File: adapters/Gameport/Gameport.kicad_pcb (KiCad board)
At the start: 2 copper layers, 58.4 x 35.6 mm, 20 parts, among them J1 Port 1, J2 Port 2, J3 Gameport, M1 Mounting, M2 Mounting, M3 Mounting, M4 Mounting, Q1 BC557, Q2 BC557

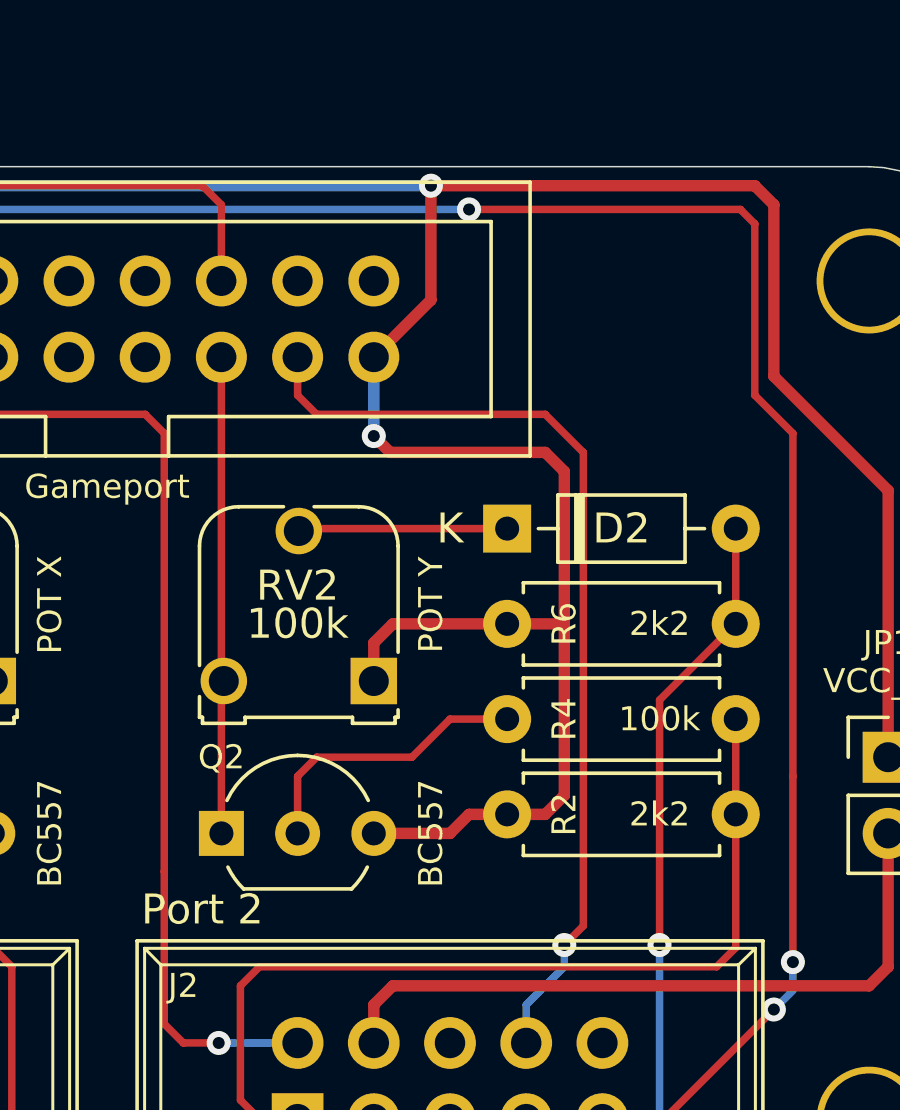
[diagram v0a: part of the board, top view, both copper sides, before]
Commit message: Fixed pin linked to VCC
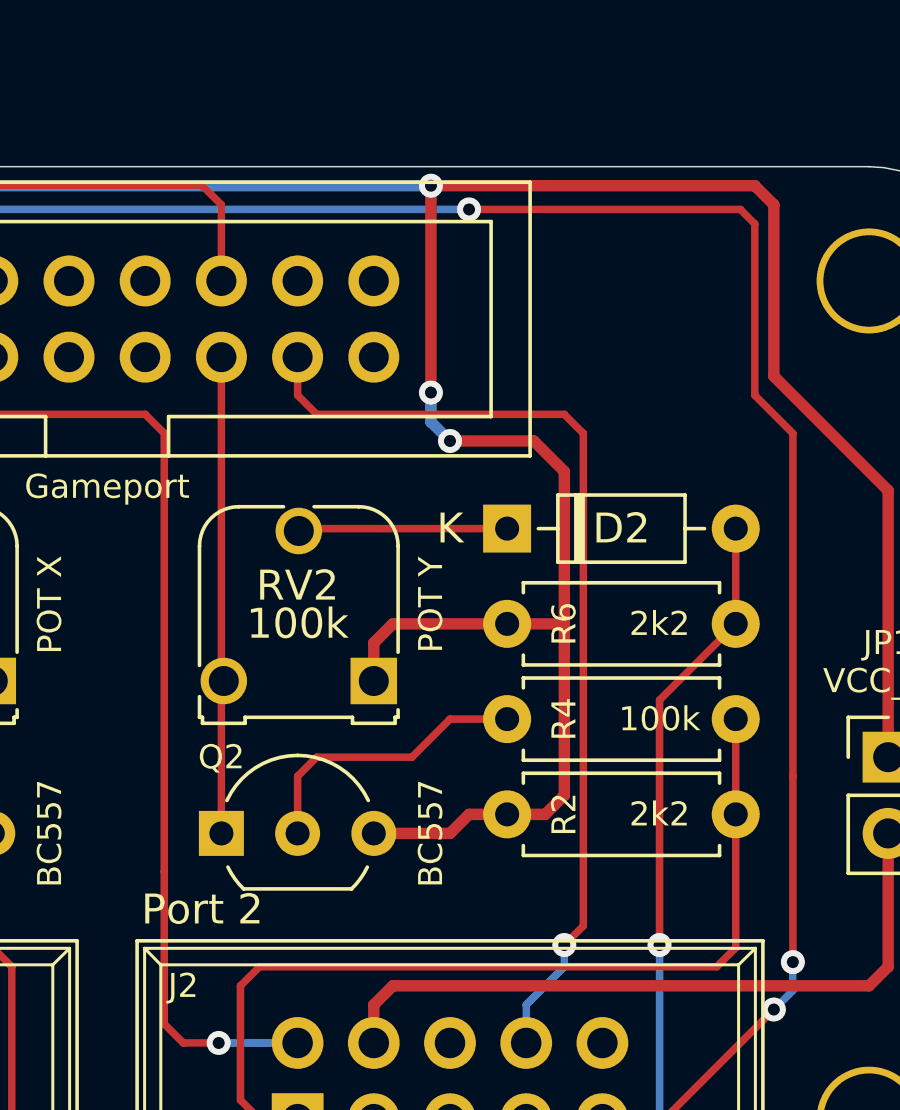
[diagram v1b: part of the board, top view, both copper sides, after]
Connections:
- J3 pad 8: VCC -> (no net)
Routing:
- net VCC: track 149.1 -> 146.1 mm, vias 2 -> 3

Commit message: Trying out different circuit
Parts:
- removed RV1, RV2: 100k, RM-065:RM-065
- added R7: 100k, resistor:R_Axial_DIN0207_L6.3mm_D2.5mm_P7.62mm_Horizontal, F.Cu at (120.0, 92.7)
- added R8: 100k, resistor:R_Axial_DIN0207_L6.3mm_D2.5mm_P7.62mm_Horizontal, F.Cu at (160.7, 92.7)
- Q1, Q2: value BC557 -> 2N3906
- R1, R2: value 2k2 -> 100k
- R5, R6: value 2k2 -> 47k
- moved R2 11.9 mm to (160.7, 86.4)
- moved R6 11.7 mm to (168.3, 95.9), turned to 180 degrees
- moved D1 7.62 mm to (130.8, 95.9), turned to 90 degrees
- moved D2 7.62 mm to (157.5, 95.9), turned to 90 degrees
- moved Q1 7.62 mm to (135.3, 90.8)
- moved Q2 7.62 mm to (148.0, 90.8)
- moved R4 5.99 mm to (160.7, 89.5)
- moved R1 5.99 mm to (120.0, 86.4)
- moved R3 5.99 mm to (120.0, 89.5)
- moved JP1 3.81 mm to (170.2, 99.7)
- moved R5 3.70 mm to (120.0, 95.9)
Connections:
- J3 pad 3: Net-(J3-Pad3) -> Net-(D1-Pad1)
- J3 pad 6: Net-(J3-Pad6) -> Net-(D2-Pad1)
- J3 pad 9: VCC -> (no net)
- Q1 pad 1: Net-(J3-Pad3) -> VCC
- Q1 pad 3: VCC -> Net-(D1-Pad1)
- Q2 pad 1: Net-(J3-Pad6) -> VCC
- Q2 pad 3: VCC -> Net-(D2-Pad1)
- R1 pad 2: /JK_LEFT -> /JK_RIGHT
- R2 pad 2: /JK_UP -> /JK_DOWN
- R3 pad 1: Net-(Q1-Pad2) -> VCC
- R3 pad 2: /JK_LEFT -> Net-(D1-Pad1)
- R4 pad 1: Net-(Q2-Pad2) -> VCC
- R4 pad 2: /JK_UP -> Net-(D2-Pad1)
- R5 pad 1: VCC -> /JK_LEFT
- R5 pad 2: /JK_RIGHT -> Net-(Q1-Pad2)
- R6 pad 1: VCC -> Net-(Q2-Pad2)
- R6 pad 2: /JK_DOWN -> /JK_UP
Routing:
- net VCC: track 146.1 -> 92.4 mm, vias 3 -> 0
- net Net-(D1-Pad1): track 7.06 -> 38.1 mm
- net Net-(D2-Pad1): track 6.98 -> 33.4 mm
- net Net-(Q2-Pad2): track 9.68 -> 29.9 mm
- net Net-(J3-Pad3): track 20.2 -> 0.00 mm
- net Net-(J3-Pad6): track 15.9 -> 0.00 mm
- net /JK_DOWN: track 33.3 -> 48.8 mm
- net /JK_FIRE3: track 64.1 -> 74.2 mm, vias 3 -> 1
- net /JK_UP: track 30.6 -> 20.7 mm
- net /JK_LEFT: track 43.2 -> 52.1 mm
- net Net-(Q1-Pad2): track 22.8 -> 14.9 mm
- net /JK_FIRE2: track 32.4 -> 37.7 mm
- net Net-(J2-Pad7): track 23.4 -> 18.9 mm
- net /JK_RIGHT: track 64.4 -> 63.6 mm, vias 0 -> 1
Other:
- board text added: "PC Gameport (C64 JoyKEY Adapter) github.com/tebl"
- board text removed: "Gameport (C64 JoyKEY Adapter) github.com/tebl"
- board text removed: "POT X"
- board text removed: "POT Y"

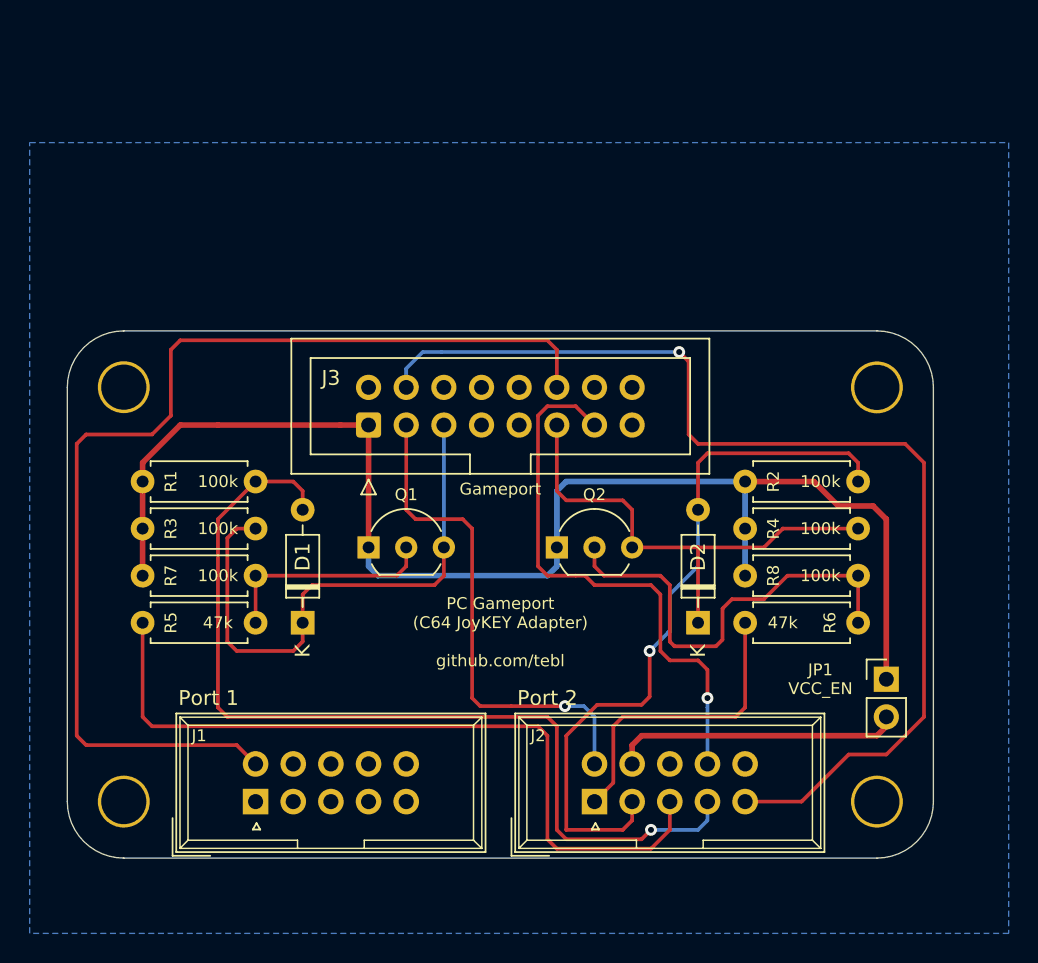
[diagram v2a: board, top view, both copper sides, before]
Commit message: Different gameport circuit
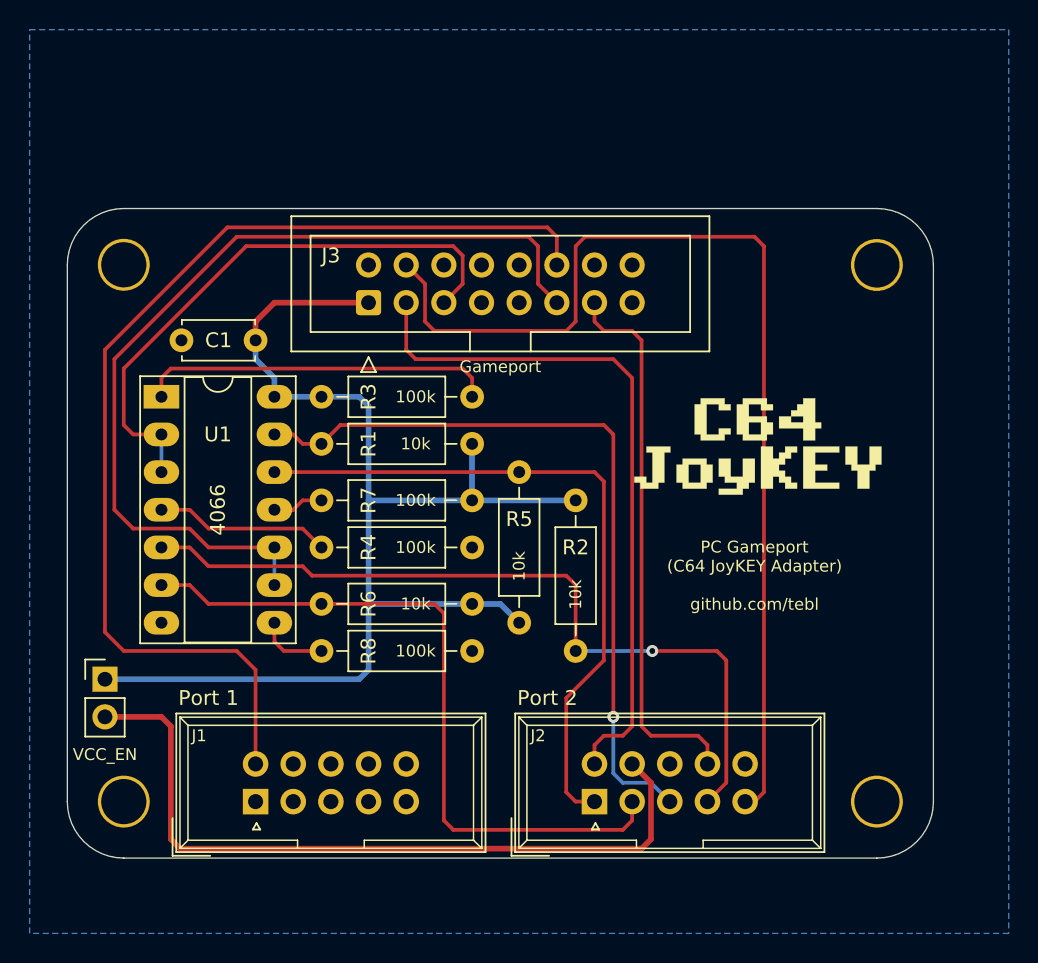
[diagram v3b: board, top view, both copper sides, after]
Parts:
- removed D1, D2: 1N4148, Diode_THT:D_DO-35_SOD27_P7.62mm_Horizontal
- removed Q1, Q2: 2N3906, Package_TO_SOT_THT:TO-92_Inline_Wide
- added C1: 100nF, Capacitor_THT:C_Disc_D4.7mm_W2.5mm_P5.00mm, F.Cu at (127.6, 76.8)
- added G***: LOGO, logo:c64_joykey, F.Cu at (161.3, 83.8)
- added U1: 4066, Package_DIP:DIP-14_W7.62mm_Socket_LongPads, F.Cu at (121.3, 80.6)
- R1, R2: value 100k -> 10k; footprint resistor:R_Axial_DIN0207_L6.3mm_D2.5mm_P7.62mm_Horizontal -> Resistor_THT:R_Axial_DIN0207_L6.3mm_D2.5mm_P10.16mm_Horizontal
- R3, R4, R7, R8: footprint resistor:R_Axial_DIN0207_L6.3mm_D2.5mm_P7.62mm_Horizontal -> Resistor_THT:R_Axial_DIN0207_L6.3mm_D2.5mm_P10.16mm_Horizontal
- R5, R6: value 47k -> 10k; footprint resistor:R_Axial_DIN0207_L6.3mm_D2.5mm_P7.62mm_Horizontal -> Resistor_THT:R_Axial_DIN0207_L6.3mm_D2.5mm_P10.16mm_Horizontal
- moved JP1 52.7 mm to (117.5, 99.7)
- moved R6 36.2 mm to (132.1, 94.6), turned to 0 degrees
- moved R5 27.4 mm to (145.4, 85.7), turned to 270 degrees
- moved R3 23.9 mm to (142.2, 80.6), turned to 180 degrees
- moved R8 19.1 mm to (142.2, 97.8), turned to 180 degrees
- moved R4 18.5 mm to (142.2, 90.8), turned to 180 degrees
- moved R2 16.2 mm to (149.2, 97.8), turned to 90 degrees
- moved R7 13.1 mm to (132.1, 87.6)
- moved R1 12.3 mm to (132.1, 83.8)
- moved M3 8.26 mm to (169.5, 71.8)
- moved J3 8.25 mm to (135.3, 74.3)
- moved M4 8.25 mm to (118.7, 71.7)
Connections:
- net /JK_FIRE1 renamed JK_FIRE1
- net /JK_FIRE2 renamed JK_FIRE2
- net /JK_FIRE3 renamed JK_FIRE3
- net /JK_FIRE4 renamed JK_FIRE4
- J2 pad 1: /JK_UP -> JK_UP
- J2 pad 2: /JK_DOWN -> JK_DOWN
- J2 pad 3: /JK_LEFT -> JK_LEFT
- J2 pad 4: /JK_RIGHT -> JK_RIGHT
- J3 pad 3: Net-(D1-Pad1) -> PC_X
- J3 pad 6: Net-(D2-Pad1) -> PC_Y
- R1 pad 1: VCC -> JK_LEFT
- R1 pad 2: /JK_RIGHT -> VCC
- R2 pad 1: VCC -> JK_RIGHT
- R2 pad 2: /JK_DOWN -> VCC
- R3 pad 1: VCC -> Net-(R3-Pad1)
- R3 pad 2: Net-(D1-Pad1) -> VCC
- R4 pad 1: VCC -> GND
- R4 pad 2: Net-(D2-Pad1) -> Net-(R4-Pad2)
- R5 pad 1: /JK_LEFT -> JK_UP
- R5 pad 2: Net-(Q1-Pad2) -> VCC
- R6 pad 1: Net-(Q2-Pad2) -> JK_DOWN
- R6 pad 2: /JK_UP -> VCC
- R7 pad 1: VCC -> Net-(R7-Pad1)
- R7 pad 2: Net-(Q1-Pad2) -> VCC
- R8 pad 1: VCC -> GND
- R8 pad 2: Net-(Q2-Pad2) -> Net-(R8-Pad2)
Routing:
- net /JK_RIGHT: track 63.6 -> 0.00 mm, vias 1 -> 0
- net PC_Y: track 0.00 -> 61.1 mm
- net JK_RIGHT: track 0.00 -> 53.9 mm, vias 0 -> 1
- net /JK_LEFT: track 52.1 -> 0.00 mm
- net JK_LEFT: track 0.00 -> 51.4 mm, vias 0 -> 1
- net /JK_DOWN: track 48.8 -> 0.00 mm, vias 1 -> 0
- net JK_DOWN: track 0.00 -> 48.3 mm
- net JK_UP: track 0.00 -> 46.7 mm
- net PC_X: track 0.00 -> 39.4 mm
- net Net-(D1-Pad1): track 38.1 -> 0.00 mm
- net Net-(D2-Pad1): track 33.4 -> 0.00 mm
- net Net-(J2-Pad7): track 18.9 -> 50.8 mm
- net Net-(Q2-Pad2): track 29.9 -> 0.00 mm
- net Net-(R3-Pad1): track 0.00 -> 24.0 mm
- net /JK_UP: track 20.7 -> 0.00 mm
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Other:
- board size 58.4 x 35.6 mm -> 58.4 x 43.8 mm

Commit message: Gameport adapter that doesn't work
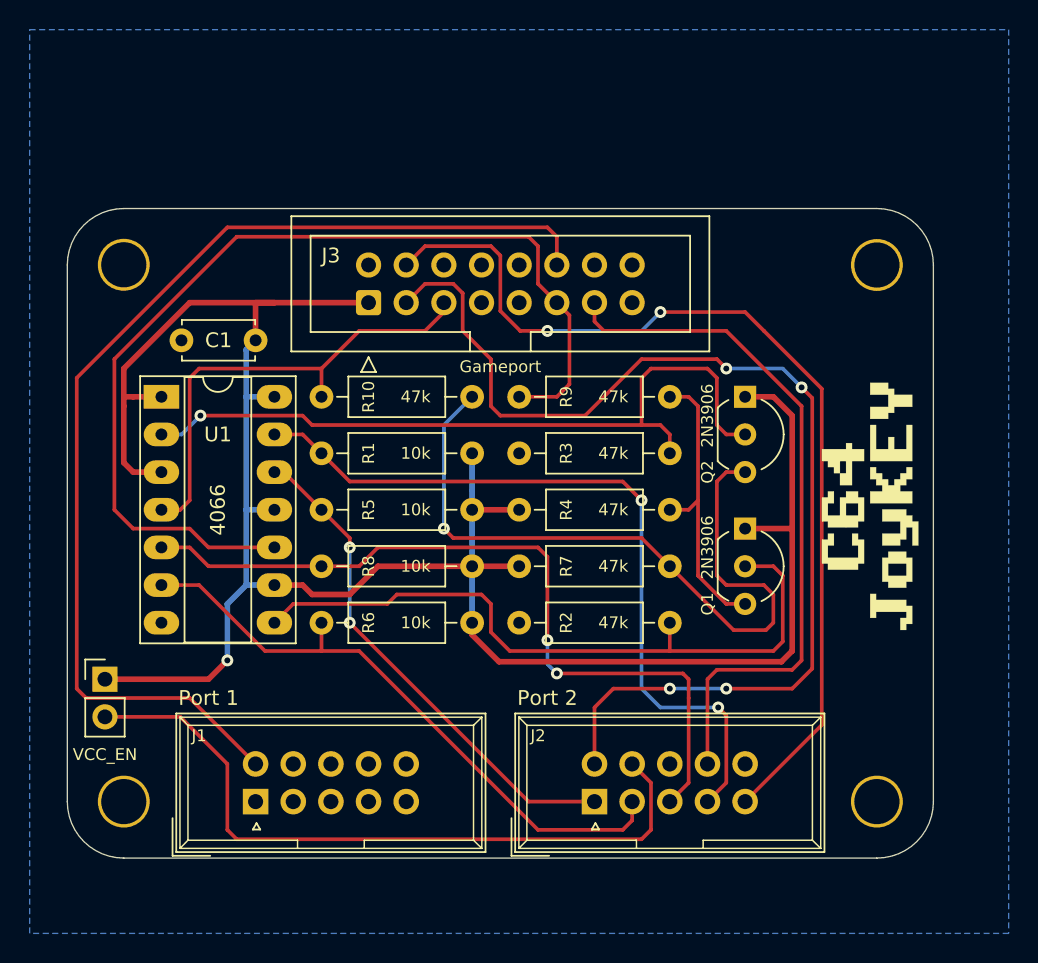
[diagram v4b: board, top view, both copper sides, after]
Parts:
- added G***: LOGO, logo:c64_joykey, F.Cu at (168.9, 88.3)
- added Q1: 2N3906, Package_TO_SOT_THT:TO-92_Inline_Wide, F.Cu at (160.7, 89.5)
- added Q2: 2N3906, Package_TO_SOT_THT:TO-92_Inline_Wide, F.Cu at (160.7, 80.6)
- added R10: 47k, Resistor_THT:R_Axial_DIN0207_L6.3mm_D2.5mm_P10.16mm_Horizontal, F.Cu at (142.2, 80.6)
- added R9: 47k, Resistor_THT:R_Axial_DIN0207_L6.3mm_D2.5mm_P10.16mm_Horizontal, F.Cu at (155.6, 80.6)
- G***: moved to B.Cu
- R2: value 10k -> 47k
- R3, R4, R7: value 100k -> 47k
- R8: value 100k -> 10k
- moved R7 14.1 mm to (145.4, 92.1)
- moved R5 13.6 mm to (132.1, 88.3), turned to 0 degrees
- moved R8 11.7 mm to (132.1, 92.1), turned to 0 degrees
- moved G*** 8.82 mm to (168.9, 88.3), turned to 90 degrees
- moved R3 4.96 mm to (145.4, 84.5), turned to 0 degrees
- moved R2 4.26 mm to (145.4, 95.9), turned to 0 degrees
- moved R4 4.07 mm to (145.4, 88.3), turned to 0 degrees
- moved R6 1.27 mm to (132.1, 95.9)
- moved R1 0.64 mm to (132.1, 84.5)
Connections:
- R1 pad 1: JK_LEFT -> JK_RIGHT
- R2 pad 1: JK_RIGHT -> GND
- R2 pad 2: VCC -> Net-(Q1-Pad2)
- R3 pad 1: Net-(R3-Pad1) -> GND
- R3 pad 2: VCC -> Net-(Q2-Pad2)
- R4 pad 1: GND -> VCC
- R4 pad 2: Net-(R4-Pad2) -> Net-(Q1-Pad3)
- R7 pad 1: Net-(R7-Pad1) -> VCC
- R7 pad 2: VCC -> Net-(Q2-Pad3)
- R8 pad 1: GND -> JK_LEFT
- R8 pad 2: Net-(R8-Pad2) -> VCC
- U1 pad 1: Net-(R3-Pad1) -> VCC
- U1 pad 11: Net-(R7-Pad1) -> VCC
- U1 pad 13: JK_LEFT -> JK_RIGHT
- U1 pad 2: PC_X -> Net-(Q2-Pad2)
- U1 pad 3: PC_X -> VCC
- U1 pad 4: Net-(R4-Pad2) -> PC_X
- U1 pad 5: JK_RIGHT -> JK_LEFT
- U1 pad 8: Net-(R8-Pad2) -> Net-(Q1-Pad2)
- U1 pad 9: PC_Y -> VCC
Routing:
- net VCC: track 84.7 -> 149.1 mm, vias 0 -> 1
- net Net-(Q2-Pad2): track 0.00 -> 50.7 mm, vias 0 -> 1
- net Net-(Q2-Pad3): track 0.00 -> 49.7 mm, vias 0 -> 1
- net Net-(Q1-Pad2): track 0.00 -> 47.2 mm
- net JK_FIRE1: track 47.0 -> 75.4 mm, vias 0 -> 4
- net Net-(R3-Pad1): track 24.0 -> 0.00 mm
- net Net-(Q1-Pad3): track 0.00 -> 19.7 mm
- net JK_UP: track 46.7 -> 34.1 mm, vias 0 -> 2
- net Net-(R4-Pad2): track 11.8 -> 0.00 mm
- net JK_FIRE2: track 37.2 -> 47.3 mm
- net PC_X: track 39.4 -> 31.9 mm
- net PC_Y: track 61.1 -> 68.2 mm
- net JK_DOWN: track 48.3 -> 42.0 mm
- net JK_FIRE3: track 71.7 -> 65.8 mm, vias 0 -> 2
- net Net-(R8-Pad2): track 4.71 -> 0.00 mm
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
